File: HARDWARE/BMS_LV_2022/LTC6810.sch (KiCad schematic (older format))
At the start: 32 parts, among them J10 Conn_01x01_Female, J4 Conn_01x01_Female, J5 Conn_01x01_Female, J6 Conn_01x01_Female, J7 Conn_01x01_Female, J8 Conn_01x01_Female, J9 Conn_01x01_Female, Q1 BC846

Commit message: PCB layout init
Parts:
- BT1: footprint Connector_PinHeader_2.54mm:PinHeader_1x01_P2.54mm_Vertical -> (none)
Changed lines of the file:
@@
 F 0 "BT1" H 3618 2746 50  0000 L CNN
 F 1 "Battery_Cell" H 3618 2655 50  0000 L CNN
-F 2 "Connector_PinHeader_2.54mm:PinHeader_1x01_P2.54mm_Vertical" V 3500 2710 50  0001 C CNN
+F 2 "" V 3500 2710 50  0001 C CNN
 F 3 "~" V 3500 2710 50  0001 C CNN
 	1    3500 2650

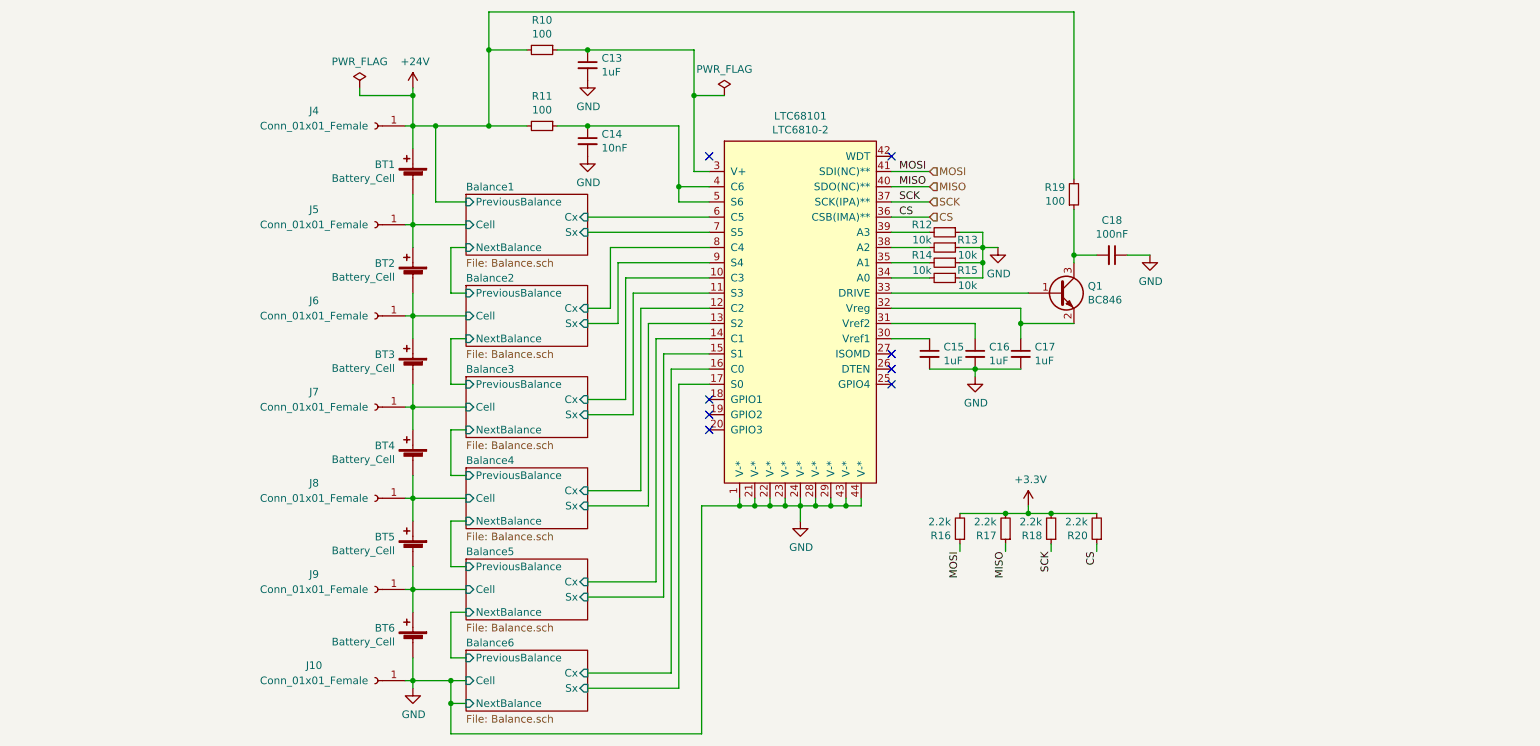
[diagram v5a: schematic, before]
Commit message: Thermistors change
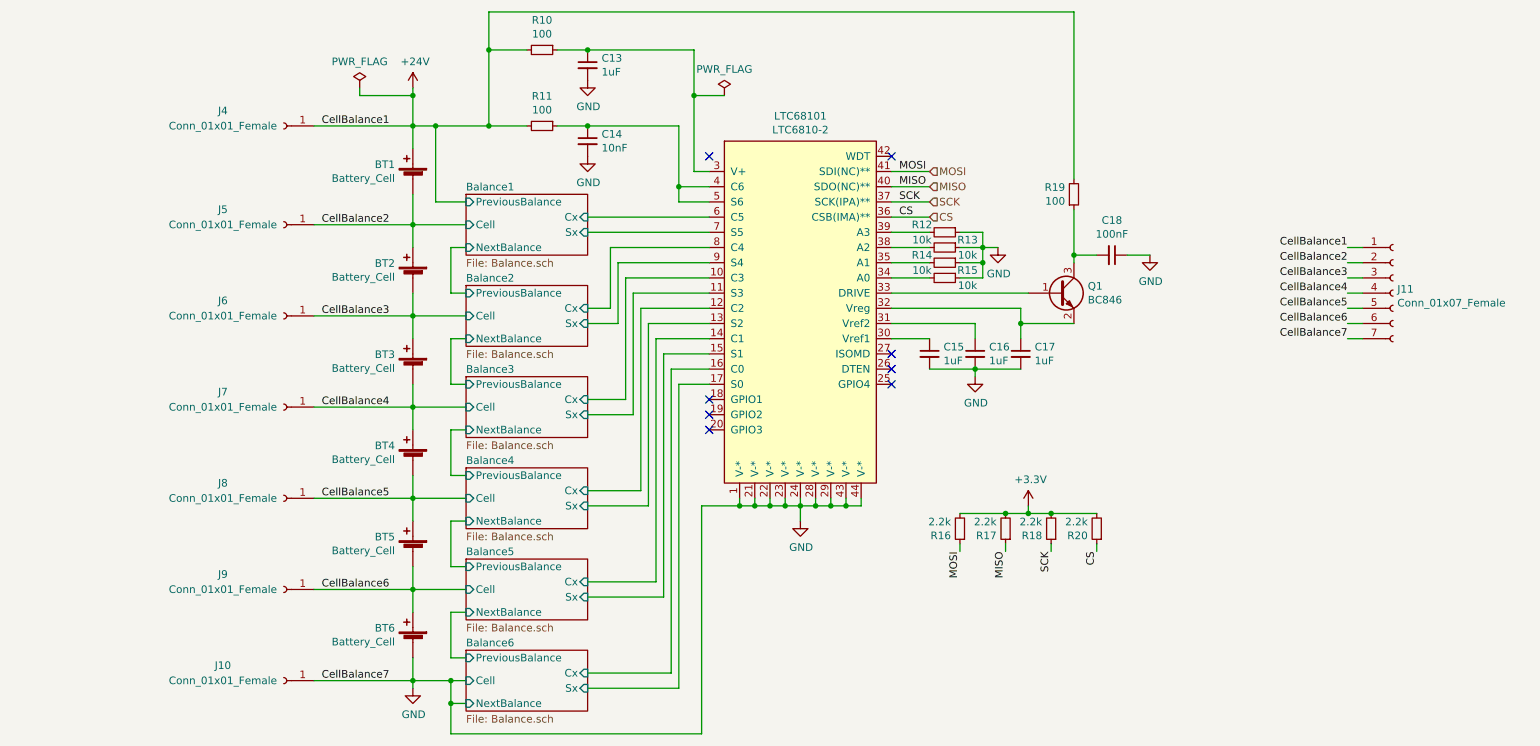
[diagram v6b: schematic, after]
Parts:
- added J11: Conn_01x07_Female, Connector_JST:JST_XH_B7B-XH-A_1x07_P2.50mm_Vertical, symbol Connector:Conn_01x07_Female
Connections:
- net +24V: now also J11.1 (Pin_1)
- net GND: now also J11.7 (Pin_7)
- net Balance1/Cell renamed CellBalance2
- net CellBalance2: now also J11.2 (Pin_2)
- net Balance2/Cell renamed CellBalance3
- net CellBalance3: now also J11.3 (Pin_3)
- net Balance3/Cell renamed CellBalance4
- net CellBalance4: now also J11.4 (Pin_4)
- net Balance4/Cell renamed CellBalance5
- net CellBalance5: now also J11.5 (Pin_5)
- net Balance5/Cell renamed CellBalance6
- net CellBalance6: now also J11.6 (Pin_6)
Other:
- moved on the sheet: J10, J4, J5, J6, J7, J8, J9
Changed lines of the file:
@@
 	1    0    0    -1
 $EndComp
-Wire Wire Line
-	3450 5950 3500 5950
-Wire Wire Line
-	3450 5350 3500 5350
-Wire Wire Line
-	3450 4750 3500 4750
-Wire Wire Line
-	3450 4150 3500 4150
-Wire Wire Line
-	3450 3550 3500 3550
-Wire Wire Line
-	3450 2950 3500 2950
-Wire Wire Line
-	3500 2300 3450 2300
 $Comp
 L Connector:Conn_01x01_Female J4
 U 1 1 61A1B6B1
-P 3250 2300
-F 0 "J4" H 3650 2400 50  0000 C CNN
-F 1 "Conn_01x01_Female" H 3650 2300 50  0000 C CNN
-F 2 "Connector_PinHeader_2.54mm:PinHeader_1x01_P2.54mm_Vertical" H 3250 2300 50  0001 C CNN
-F 3 "~" H 3250 2300 50  0001 C CNN
-	1    3250 2300
+P 2650 2300
+F 0 "J4" H 3050 2400 50  0000 C CNN
+F 1 "Conn_01x01_Female" H 3050 2300 50  0000 C CNN
+F 2 "Connector_PinHeader_2.54mm:PinHeader_1x01_P2.54mm_Vertical" H 2650 2300 50  0001 C CNN
+F 3 "~" H 2650 2300 50  0001 C CNN
+	1    2650 2300
 	-1   0    0    -1
 $EndComp
@@
 L Connector:Conn_01x01_Female J5
 U 1 1 61A336C9
-P 3250 2950
-F 0 "J5" H 3650 3050 50  0000 C CNN
-F 1 "Conn_01x01_Female" H 3650 2950 50  0000 C CNN
-F 2 "Connector_PinHeader_2.54mm:PinHeader_1x01_P2.54mm_Vertical" H 3250 2950 50  0001 C CNN
-F 3 "~" H 3250 2950 50  0001 C CNN
-	1    3250 2950
+P 2650 2950
+F 0 "J5" H 3050 3050 50  0000 C CNN
+F 1 "Conn_01x01_Female" H 3050 2950 50  0000 C CNN
+F 2 "Connector_PinHeader_2.54mm:PinHeader_1x01_P2.54mm_Vertical" H 2650 2950 50  0001 C CNN
+F 3 "~" H 2650 2950 50  0001 C CNN
+	1    2650 2950
 	-1   0    0    -1
 $EndComp
@@
 L Connector:Conn_01x01_Female J6
 U 1 1 61A9D24A
-P 3250 3550
-F 0 "J6" H 3650 3650 50  0000 C CNN
-F 1 "Conn_01x01_Female" H 3650 3550 50  0000 C CNN
-F 2 "Connector_PinHeader_2.54mm:PinHeader_1x01_P2.54mm_Vertical" H 3250 3550 50  0001 C CNN
-F 3 "~" H 3250 3550 50  0001 C CNN
-	1    3250 3550
+P 2650 3550
+F 0 "J6" H 3050 3650 50  0000 C CNN
+F 1 "Conn_01x01_Female" H 3050 3550 50  0000 C CNN
+F 2 "Connector_PinHeader_2.54mm:PinHeader_1x01_P2.54mm_Vertical" H 2650 3550 50  0001 C CNN
+F 3 "~" H 2650 3550 50  0001 C CNN
+	1    2650 3550
 	-1   0    0    -1
 $EndComp
@@
 L Connector:Conn_01x01_Female J7
 U 1 1 61AA88B9
-P 3250 4150
-F 0 "J7" H 3650 4250 50  0000 C CNN
-F 1 "Conn_01x01_Female" H 3650 4150 50  0000 C CNN
-F 2 "Connector_PinHeader_2.54mm:PinHeader_1x01_P2.54mm_Vertical" H 3250 4150 50  0001 C CNN
-F 3 "~" H 3250 4150 50  0001 C CNN
-	1    3250 4150
+P 2650 4150
+F 0 "J7" H 3050 4250 50  0000 C CNN
+F 1 "Conn_01x01_Female" H 3050 4150 50  0000 C CNN
+F 2 "Connector_PinHeader_2.54mm:PinHeader_1x01_P2.54mm_Vertical" H 2650 4150 50  0001 C CNN
+F 3 "~" H 2650 4150 50  0001 C CNN
+	1    2650 4150
 	-1   0    0    -1
 $EndComp
@@
 L Connector:Conn_01x01_Female J8
 U 1 1 61AAC32A
-P 3250 4750
-F 0 "J8" H 3650 4850 50  0000 C CNN
-F 1 "Conn_01x01_Female" H 3650 4750 50  0000 C CNN
-F 2 "Connector_PinHeader_2.54mm:PinHeader_1x01_P2.54mm_Vertical" H 3250 4750 50  0001 C CNN
-F 3 "~" H 3250 4750 50  0001 C CNN
-	1    3250 4750
+P 2650 4750
+F 0 "J8" H 3050 4850 50  0000 C CNN
+F 1 "Conn_01x01_Female" H 3050 4750 50  0000 C CNN
+F 2 "Connector_PinHeader_2.54mm:PinHeader_1x01_P2.54mm_Vertical" H 2650 4750 50  0001 C CNN
+F 3 "~" H 2650 4750 50  0001 C CNN
+	1    2650 4750
 	-1   0    0    -1
 $EndComp
@@
 L Connector:Conn_01x01_Female J9
 U 1 1 61AAFFF2
-P 3250 5350
-F 0 "J9" H 3650 5450 50  0000 C CNN
-F 1 "Conn_01x01_Female" H 3650 5350 50  0000 C CNN
-F 2 "Connector_PinHeader_2.54mm:PinHeader_1x01_P2.54mm_Vertical" H 3250 5350 50  0001 C CNN
-F 3 "~" H 3250 5350 50  0001 C CNN
-	1    3250 5350
+P 2650 5350
+F 0 "J9" H 3050 5450 50  0000 C CNN
+F 1 "Conn_01x01_Female" H 3050 5350 50  0000 C CNN
+F 2 "Connector_PinHeader_2.54mm:PinHeader_1x01_P2.54mm_Vertical" H 2650 5350 50  0001 C CNN
+F 3 "~" H 2650 5350 50  0001 C CNN
+	1    2650 5350
 	-1   0    0    -1
 $EndComp
@@
 L Connector:Conn_01x01_Female J10
 U 1 1 61AB3B1A
-P 3250 5950
-F 0 "J10" H 3650 6050 50  0000 C CNN
-F 1 "Conn_01x01_Female" H 3650 5950 50  0000 C CNN
-F 2 "Connector_PinHeader_2.54mm:PinHeader_1x01_P2.54mm_Vertical" H 3250 5950 50  0001 C CNN
-F 3 "~" H 3250 5950 50  0001 C CNN
-	1    3250 5950
+P 2650 5950
+F 0 "J10" H 3050 6050 50  0000 C CNN
+F 1 "Conn_01x01_Female" H 3050 5950 50  0000 C CNN
+F 2 "Connector_PinHeader_2.54mm:PinHeader_1x01_P2.54mm_Vertical" H 2650 5950 50  0001 C CNN
+F 3 "~" H 2650 5950 50  0001 C CNN
+	1    2650 5950
 	-1   0    0    -1
 $EndComp
@@
 	1    0    0    -1
 $EndComp
+Wire Wire Line
+	2850 5950 3500 5950
+Wire Wire Line
+	2850 2950 3500 2950
+Wire Wire Line
+	2850 2300 3500 2300
+Wire Wire Line
+	2850 3550 3500 3550
+Wire Wire Line
+	2850 4150 3500 4150
+Wire Wire Line
+	2850 4750 3500 4750
+Wire Wire Line
+	2850 5350 3500 5350
+Text Label 2900 2300 0    50   ~ 0
+CellBalance1
+Text Label 2900 2950 0    50   ~ 0
+CellBalance2
+Text Label 2900 3550 0    50   ~ 0
+CellBalance3
+Text Label 2900 4150 0    50   ~ 0
+CellBalance4
+Text Label 2900 4750 0    50   ~ 0
+CellBalance5
+Text Label 2900 5350 0    50   ~ 0
+CellBalance6
+Text Label 2900 5950 0    50   ~ 0
+CellBalance7
+Text Label 9650 3100 2    50   ~ 0
+CellBalance1
+Text Label 9650 3200 2    50   ~ 0
+CellBalance2
+Text Label 9650 3300 2    50   ~ 0
+CellBalance3
+Text Label 9650 3400 2    50   ~ 0
+CellBalance4
+Text Label 9650 3500 2    50   ~ 0
+CellBalance5
+Text Label 9650 3600 2    50   ~ 0
+CellBalance6
+Text Label 9650 3700 2    50   ~ 0
+CellBalance7
+$Comp
+L Connector:Conn_01x07_Female J11
+U 1 1 61DCAD61
+P 9950 3400
+F 0 "J11" H 9978 3426 50  0000 L CNN
+F 1 "Conn_01x07_Female" H 9978 3335 50  0000 L CNN
+F 2 "Connector_JST:JST_XH_B7B-XH-A_1x07_P2.50mm_Vertical" H 9950 3400 50  0001 C CNN
+F 3 "~" H 9950 3400 50  0001 C CNN
+	1    9950 3400
+	1    0    0    -1
+$EndComp
+Wire Wire Line
+	9650 3100 9750 3100
+Wire Wire Line
+	9650 3200 9750 3200
+Wire Wire Line
+	9650 3300 9750 3300
+Wire Wire Line
+	9650 3400 9750 3400
+Wire Wire Line
+	9650 3500 9750 3500
+Wire Wire Line
+	9650 3600 9750 3600
+Wire Wire Line
+	9650 3700 9750 3700
 $EndSCHEMATC

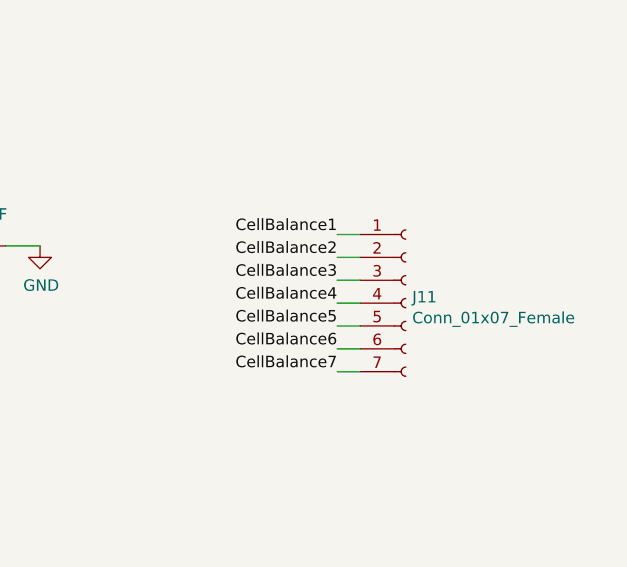
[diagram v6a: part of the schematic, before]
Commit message: PCB update
Parts changed due to smaller footprints
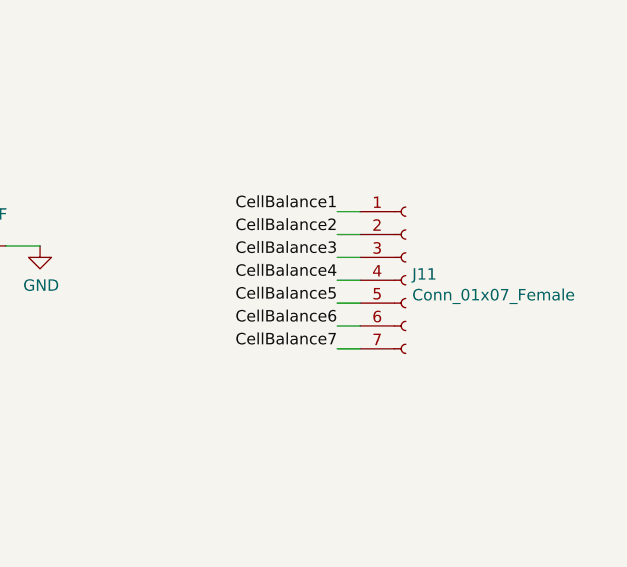
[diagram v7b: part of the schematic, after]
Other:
- moved on the sheet: J11
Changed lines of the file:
@@
 Text Label 2900 5950 0    50   ~ 0
 CellBalance7
+Text Label 9650 3000 2    50   ~ 0
+CellBalance1
 Text Label 9650 3100 2    50   ~ 0
-CellBalance1
+CellBalance2
 Text Label 9650 3200 2    50   ~ 0
-CellBalance2
+CellBalance3
 Text Label 9650 3300 2    50   ~ 0
-CellBalance3
+CellBalance4
 Text Label 9650 3400 2    50   ~ 0
-CellBalance4
+CellBalance5
 Text Label 9650 3500 2    50   ~ 0
-CellBalance5
+CellBalance6
 Text Label 9650 3600 2    50   ~ 0
-CellBalance6
-Text Label 9650 3700 2    50   ~ 0
 CellBalance7
 $Comp
 L Connector:Conn_01x07_Female J11
 U 1 1 61DCAD61
-P 9950 3400
-F 0 "J11" H 9978 3426 50  0000 L CNN
-F 1 "Conn_01x07_Female" H 9978 3335 50  0000 L CNN
-F 2 "Connector_JST:JST_XH_B7B-XH-A_1x07_P2.50mm_Vertical" H 9950 3400 50  0001 C CNN
-F 3 "~" H 9950 3400 50  0001 C CNN
-	1    9950 3400
+P 9950 3300
+F 0 "J11" H 9978 3326 50  0000 L CNN
+F 1 "Conn_01x07_Female" H 9978 3235 50  0000 L CNN
+F 2 "Connector_JST:JST_XH_B7B-XH-A_1x07_P2.50mm_Vertical" H 9950 3300 50  0001 C CNN
+F 3 "~" H 9950 3300 50  0001 C CNN
+	1    9950 3300
 	1    0    0    -1
 $EndComp
+Wire Wire Line
+	9650 3000 9750 3000
 Wire Wire Line
 	9650 3100 9750 3100
@@
 Wire Wire Line
 	9650 3600 9750 3600
-Wire Wire Line
-	9650 3700 9750 3700
 $EndSCHEMATC
